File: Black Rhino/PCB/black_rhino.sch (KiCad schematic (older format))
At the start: 174 parts, among them SW1 SW_Push, U1 ATmega32U4-AU, Y1 16MHz

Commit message: Improve Black Rhino-PCB
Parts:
- added H23: MountingHole, MountingHole:MountingHole_2mm, symbol Mechanical:MountingHole
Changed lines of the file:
@@
 Wire Wire Line
 	19900 2900 20650 2900
+$Comp
+L Mechanical:MountingHole H23
+U 1 1 5F2CFA80
+P 19300 13400
+F 0 "H23" H 19400 13446 50  0000 L CNN
+F 1 "MountingHole" H 19400 13355 50  0000 L CNN
+F 2 "MountingHole:MountingHole_2mm" H 19300 13400 50  0001 C CNN
+F 3 "~" H 19300 13400 50  0001 C CNN
+	1    19300 13400
+	1    0    0    -1
+$EndComp
 $EndSCHEMATC

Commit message: Improve Black Rhino-PCB
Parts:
- removed H13, H14, H15, H16, H17, H18, H19, H20, H21, H22, H23: MountingHole, MountingHole:MountingHole_2mm, symbol Mechanical:MountingHole
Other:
- moved on the sheet: H10, H11, H12, H7, H8, H9
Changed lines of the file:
@@
 L Mechanical:MountingHole H7
 U 1 1 5F2A8030
-P 19300 12150
-F 0 "H7" H 19400 12196 50  0000 L CNN
-F 1 "MountingHole" H 19400 12105 50  0000 L CNN
-F 2 "MountingHole:MountingHole_2mm" H 19300 12150 50  0001 C CNN
-F 3 "~" H 19300 12150 50  0001 C CNN
-	1    19300 12150
+P 20100 10650
+F 0 "H7" H 20200 10696 50  0000 L CNN
+F 1 "MountingHole" H 20200 10605 50  0000 L CNN
+F 2 "MountingHole:MountingHole_2mm" H 20100 10650 50  0001 C CNN
+F 3 "~" H 20100 10650 50  0001 C CNN
+	1    20100 10650
 	1    0    0    -1
 $EndComp
@@
 L Mechanical:MountingHole H8
 U 1 1 5F2B82E0
-P 19300 12400
-F 0 "H8" H 19400 12446 50  0000 L CNN
-F 1 "MountingHole" H 19400 12355 50  0000 L CNN
-F 2 "MountingHole:MountingHole_2mm" H 19300 12400 50  0001 C CNN
-F 3 "~" H 19300 12400 50  0001 C CNN
-	1    19300 12400
+P 20100 10900
+F 0 "H8" H 20200 10946 50  0000 L CNN
+F 1 "MountingHole" H 20200 10855 50  0000 L CNN
+F 2 "MountingHole:MountingHole_2mm" H 20100 10900 50  0001 C CNN
+F 3 "~" H 20100 10900 50  0001 C CNN
+	1    20100 10900
 	1    0    0    -1
 $EndComp
@@
 L Mechanical:MountingHole H9
 U 1 1 5F316618
-P 20300 10650
-F 0 "H9" H 20400 10696 50  0000 L CNN
-F 1 "MountingHole" H 20400 10605 50  0000 L CNN
-F 2 "MountingHole:MountingHole_2mm" H 20300 10650 50  0001 C CNN
-F 3 "~" H 20300 10650 50  0001 C CNN
-	1    20300 10650
+P 20100 11150
+F 0 "H9" H 20200 11196 50  0000 L CNN
+F 1 "MountingHole" H 20200 11105 50  0000 L CNN
+F 2 "MountingHole:MountingHole_2mm" H 20100 11150 50  0001 C CNN
+F 3 "~" H 20100 11150 50  0001 C CNN
+	1    20100 11150
 	1    0    0    -1
 $EndComp
@@
 L Mechanical:MountingHole H10
 U 1 1 5F31661E
-P 20300 10900
-F 0 "H10" H 20400 10946 50  0000 L CNN
-F 1 "MountingHole" H 20400 10855 50  0000 L CNN
-F 2 "MountingHole:MountingHole_2mm" H 20300 10900 50  0001 C CNN
-F 3 "~" H 20300 10900 50  0001 C CNN
-	1    20300 10900
+P 20100 11400
+F 0 "H10" H 20200 11446 50  0000 L CNN
+F 1 "MountingHole" H 20200 11355 50  0000 L CNN
+F 2 "MountingHole:MountingHole_2mm" H 20100 11400 50  0001 C CNN
+F 3 "~" H 20100 11400 50  0001 C CNN
+	1    20100 11400
 	1    0    0    -1
 $EndComp
@@
 L Mechanical:MountingHole H11
 U 1 1 5F316624
-P 20300 11150
-F 0 "H11" H 20400 11196 50  0000 L CNN
-F 1 "MountingHole" H 20400 11105 50  0000 L CNN
-F 2 "MountingHole:MountingHole_2mm" H 20300 11150 50  0001 C CNN
-F 3 "~" H 20300 11150 50  0001 C CNN
-	1    20300 11150
+P 20100 11650
+F 0 "H11" H 20200 11696 50  0000 L CNN
+F 1 "MountingHole" H 20200 11605 50  0000 L CNN
+F 2 "MountingHole:MountingHole_2mm" H 20100 11650 50  0001 C CNN
+F 3 "~" H 20100 11650 50  0001 C CNN
+	1    20100 11650
 	1    0    0    -1
 $EndComp
@@
 L Mechanical:MountingHole H12
 U 1 1 5F31662A
-P 20300 11400
-F 0 "H12" H 20400 11446 50  0000 L CNN
-F 1 "MountingHole" H 20400 11355 50  0000 L CNN
-F 2 "MountingHole:MountingHole_2mm" H 20300 11400 50  0001 C CNN
-F 3 "~" H 20300 11400 50  0001 C CNN
-	1    20300 11400
-	1    0    0    -1
-$EndComp
-$Comp
-L Mechanical:MountingHole H13
-U 1 1 5F316630
-P 20300 11650
-F 0 "H13" H 20400 11696 50  0000 L CNN
-F 1 "MountingHole" H 20400 11605 50  0000 L CNN
-F 2 "MountingHole:MountingHole_2mm" H 20300 11650 50  0001 C CNN
-F 3 "~" H 20300 11650 50  0001 C CNN
-	1    20300 11650
-	1    0    0    -1
-$EndComp
-$Comp
-L Mechanical:MountingHole H14
-U 1 1 5F316636
-P 20300 11900
-F 0 "H14" H 20400 11946 50  0000 L CNN
-F 1 "MountingHole" H 20400 11855 50  0000 L CNN
-F 2 "MountingHole:MountingHole_2mm" H 20300 11900 50  0001 C CNN
-F 3 "~" H 20300 11900 50  0001 C CNN
-	1    20300 11900
-	1    0    0    -1
-$EndComp
-$Comp
-L Mechanical:MountingHole H15
-U 1 1 5F31663C
-P 20300 12150
-F 0 "H15" H 20400 12196 50  0000 L CNN
-F 1 "MountingHole" H 20400 12105 50  0000 L CNN
-F 2 "MountingHole:MountingHole_2mm" H 20300 12150 50  0001 C CNN
-F 3 "~" H 20300 12150 50  0001 C CNN
-	1    20300 12150
-	1    0    0    -1
-$EndComp
-$Comp
-L Mechanical:MountingHole H16
-U 1 1 5F316642
-P 20300 12400
-F 0 "H16" H 20400 12446 50  0000 L CNN
-F 1 "MountingHole" H 20400 12355 50  0000 L CNN
-F 2 "MountingHole:MountingHole_2mm" H 20300 12400 50  0001 C CNN
-F 3 "~" H 20300 12400 50  0001 C CNN
-	1    20300 12400
-	1    0    0    -1
-$EndComp
-$Comp
-L Mechanical:MountingHole H17
-U 1 1 5F34FFBE
-P 19300 12650
-F 0 "H17" H 19400 12696 50  0000 L CNN
-F 1 "MountingHole" H 19400 12605 50  0000 L CNN
-F 2 "MountingHole:MountingHole_2mm" H 19300 12650 50  0001 C CNN
-F 3 "~" H 19300 12650 50  0001 C CNN
-	1    19300 12650
-	1    0    0    -1
-$EndComp
-$Comp
-L Mechanical:MountingHole H18
-U 1 1 5F34FFC4
-P 20300 12650
-F 0 "H18" H 20400 12696 50  0000 L CNN
-F 1 "MountingHole" H 20400 12605 50  0000 L CNN
-F 2 "MountingHole:MountingHole_2mm" H 20300 12650 50  0001 C CNN
-F 3 "~" H 20300 12650 50  0001 C CNN
-	1    20300 12650
-	1    0    0    -1
-$EndComp
-$Comp
-L Mechanical:MountingHole H19
-U 1 1 5F37F0C0
-P 19300 12900
-F 0 "H19" H 19400 12946 50  0000 L CNN
-F 1 "MountingHole" H 19400 12855 50  0000 L CNN
-F 2 "MountingHole:MountingHole_2mm" H 19300 12900 50  0001 C CNN
-F 3 "~" H 19300 12900 50  0001 C CNN
-	1    19300 12900
-	1    0    0    -1
-$EndComp
-$Comp
-L Mechanical:MountingHole H20
-U 1 1 5F37F0C6
-P 20300 12900
-F 0 "H20" H 20400 12946 50  0000 L CNN
-F 1 "MountingHole" H 20400 12855 50  0000 L CNN
-F 2 "MountingHole:MountingHole_2mm" H 20300 12900 50  0001 C CNN
-F 3 "~" H 20300 12900 50  0001 C CNN
-	1    20300 12900
-	1    0    0    -1
-$EndComp
-$Comp
-L Mechanical:MountingHole H21
-U 1 1 5F3B30CA
-P 19300 13150
-F 0 "H21" H 19400 13196 50  0000 L CNN
-F 1 "MountingHole" H 19400 13105 50  0000 L CNN
-F 2 "MountingHole:MountingHole_2mm" H 19300 13150 50  0001 C CNN
-F 3 "~" H 19300 13150 50  0001 C CNN
-	1    19300 13150
-	1    0    0    -1
-$EndComp
-$Comp
-L Mechanical:MountingHole H22
-U 1 1 5F251A42
-P 20300 13150
-F 0 "H22" H 20400 13196 50  0000 L CNN
-F 1 "MountingHole" H 20400 13105 50  0000 L CNN
-F 2 "MountingHole:MountingHole_2mm" H 20300 13150 50  0001 C CNN
-F 3 "~" H 20300 13150 50  0001 C CNN
-	1    20300 13150
+P 20100 11900
+F 0 "H12" H 20200 11946 50  0000 L CNN
+F 1 "MountingHole" H 20200 11855 50  0000 L CNN
+F 2 "MountingHole:MountingHole_2mm" H 20100 11900 50  0001 C CNN
+F 3 "~" H 20100 11900 50  0001 C CNN
+	1    20100 11900
 	1    0    0    -1
 $EndComp
@@
 Wire Wire Line
 	19900 2900 20650 2900
-$Comp
-L Mechanical:MountingHole H23
-U 1 1 5F2CFA80
-P 19300 13400
-F 0 "H23" H 19400 13446 50  0000 L CNN
-F 1 "MountingHole" H 19400 13355 50  0000 L CNN
-F 2 "MountingHole:MountingHole_2mm" H 19300 13400 50  0001 C CNN
-F 3 "~" H 19300 13400 50  0001 C CNN
-	1    19300 13400
-	1    0    0    -1
-$EndComp
 $EndSCHEMATC

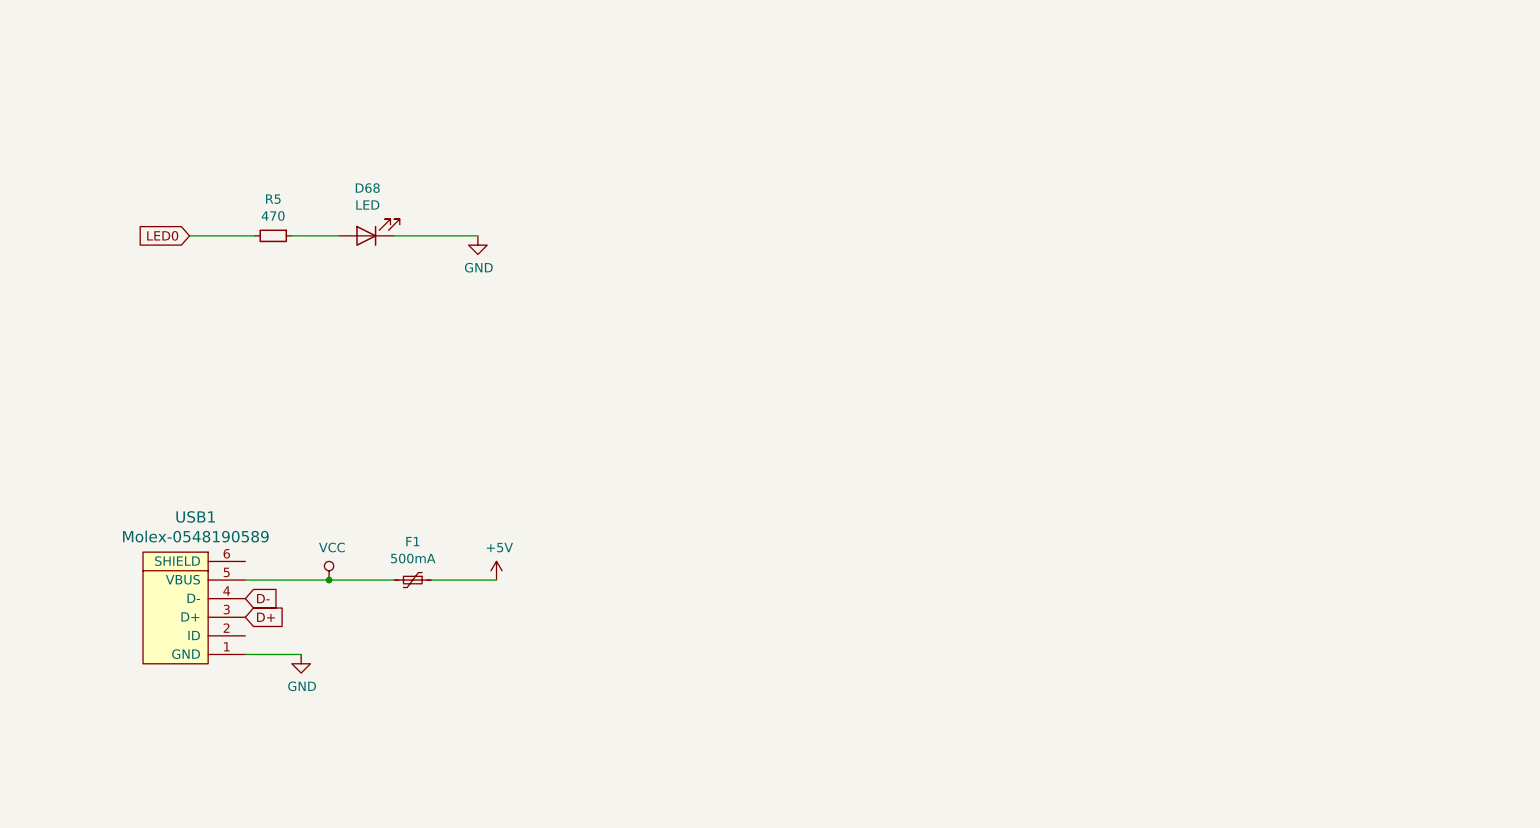
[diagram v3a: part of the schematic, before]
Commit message: Add USB-C to Black Rhino
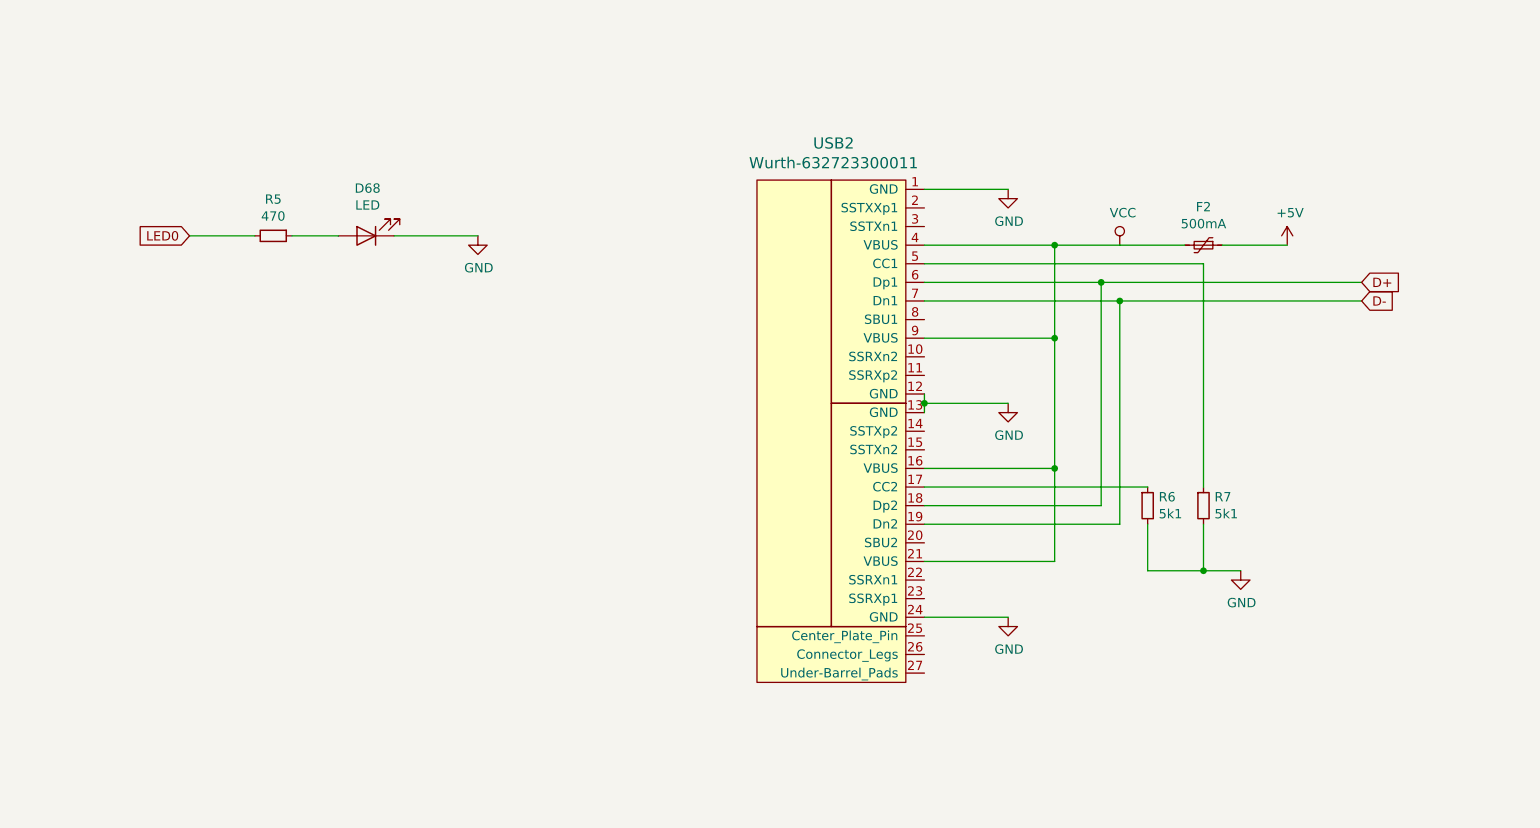
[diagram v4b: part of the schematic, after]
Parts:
- removed F1: 500mA, Fuse:Fuse_1206_3216Metric, symbol Device:Polyfuse_Small
- removed USB1: Molex-0548190589, random-keyboard-parts:Molex-0548190589, symbol random-keyboard-parts:Molex-0548190589
- added F2: 500mA, Fuse:Fuse_1206_3216Metric, symbol Device:Polyfuse_Small
- added R6, R7: 5k1, Resistor_SMD:R_0805_2012Metric, symbol Device:R_Small
- added USB2: Wurth-632723300011, Type-C:Wurth-632723300011, symbol Type-C:Wurth-632723300011
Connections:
- net +5V: now also F2.1
- net D+: now also USB2.18 (Dp2), USB2.6 (Dp1)
- net D-: now also USB2.19 (Dn2), USB2.7 (Dn1)
- net GND: now also R6.2, R7.2, USB2.1 (GND), USB2.12 (GND), USB2.13 (GND), USB2.24 (GND)
- net VCC: now also F2.2, USB2.16 (VBUS), USB2.21 (VBUS), USB2.4 (VBUS), USB2.9 (VBUS)
- new net: R6.1, USB2.17 (CC2)
- new net: R7.1, USB2.5 (CC1)
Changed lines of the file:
@@
 COL0
-Wire Wire Line
-	3250 10050 3550 10050
-$Comp
-L power:GND #PWR0113
-U 1 1 5F26C44D
-P 3550 10050
-F 0 "#PWR0113" H 3550 9800 50  0001 C CNN
-F 1 "GND" H 3555 9877 50  0000 C CNN
-F 2 "" H 3550 10050 50  0001 C CNN
-F 3 "" H 3550 10050 50  0001 C CNN
-	1    3550 10050
-	1    0    0    -1
-$EndComp
-Text GLabel 3250 9850 2    50   Input ~ 0
-D+
-Text GLabel 3250 9750 2    50   Input ~ 0
-D-
-Wire Wire Line
-	4600 9650 4250 9650
-$Comp
-L power:+5V #PWR0112
-U 1 1 5F26AF92
-P 4600 9650
-F 0 "#PWR0112" H 4600 9500 50  0001 C CNN
-F 1 "+5V" H 4615 9823 50  0000 C CNN
-F 2 "" H 4600 9650 50  0001 C CNN
-F 3 "" H 4600 9650 50  0001 C CNN
-	1    4600 9650
-	1    0    0    -1
-$EndComp
-Connection ~ 3700 9650
-Wire Wire Line
-	4050 9650 3700 9650
-$Comp
-L Device:Polyfuse_Small F1
-U 1 1 5F269C41
-P 4150 9650
-F 0 "F1" V 3945 9650 50  0000 C CNN
-F 1 "500mA" V 4036 9650 50  0000 C CNN
-F 2 "Fuse:Fuse_1206_3216Metric" H 4200 9450 50  0001 L CNN
-F 3 "~" H 4150 9650 50  0001 C CNN
-	1    4150 9650
-	0    1    1    0
-$EndComp
-Wire Wire Line
-	3250 9650 3700 9650
-$Comp
-L power:VCC #PWR0111
-U 1 1 5F268111
-P 3700 9650
-F 0 "#PWR0111" H 3700 9500 50  0001 C CNN
-F 1 "VCC" H 3717 9823 50  0000 C CNN
-F 2 "" H 3700 9650 50  0001 C CNN
-F 3 "" H 3700 9650 50  0001 C CNN
-	1    3700 9650
-	1    0    0    -1
-$EndComp
-$Comp
-L random-keyboard-parts:Molex-0548190589 USB1
-U 1 1 5F267617
-P 2950 9850
-F 0 "USB1" V 3487 9817 60  0000 C CNN
-F 1 "Molex-0548190589" V 3381 9817 60  0000 C CNN
-F 2 "random-keyboard-parts:Molex-0548190589" H 2950 9850 60  0001 C CNN
-F 3 "" H 2950 9850 60  0001 C CNN
-	1    2950 9850
-	0    -1   -1   0
-$EndComp
 Wire Wire Line
 	4050 1500 4050 1650
@@
 	-1   0    0    1
 $EndComp
+$Comp
+L power:GND #PWR0115
+U 1 1 5F3AC971
+P 7350 7550
+F 0 "#PWR0115" H 7350 7300 50  0001 C CNN
+F 1 "GND" H 7355 7377 50  0000 C CNN
+F 2 "" H 7350 7550 50  0001 C CNN
+F 3 "" H 7350 7550 50  0001 C CNN
+	1    7350 7550
+	1    0    0    -1
+$EndComp
+Wire Wire Line
+	6900 8750 6900 8700
+$Comp
+L power:GND #PWR0116
+U 1 1 5F3D340E
+P 7350 8700
+F 0 "#PWR0116" H 7350 8450 50  0001 C CNN
+F 1 "GND" H 7355 8527 50  0000 C CNN
+F 2 "" H 7350 8700 50  0001 C CNN
+F 3 "" H 7350 8700 50  0001 C CNN
+	1    7350 8700
+	1    0    0    -1
+$EndComp
+$Comp
+L power:GND #PWR0117
+U 1 1 5F3E6939
+P 7350 9850
+F 0 "#PWR0117" H 7350 9600 50  0001 C CNN
+F 1 "GND" H 7355 9677 50  0000 C CNN
+F 2 "" H 7350 9850 50  0001 C CNN
+F 3 "" H 7350 9850 50  0001 C CNN
+	1    7350 9850
+	1    0    0    -1
+$EndComp
+Wire Wire Line
+	6900 9850 7350 9850
+Wire Wire Line
+	6900 7550 7350 7550
+Wire Wire Line
+	6900 8700 7350 8700
+Connection ~ 6900 8700
+Wire Wire Line
+	6900 8700 6900 8650
+$Comp
+L power:VCC #PWR0118
+U 1 1 5F49CF34
+P 7950 7850
+F 0 "#PWR0118" H 7950 7700 50  0001 C CNN
+F 1 "VCC" H 7967 8023 50  0000 C CNN
+F 2 "" H 7950 7850 50  0001 C CNN
+F 3 "" H 7950 7850 50  0001 C CNN
+	1    7950 7850
+	1    0    0    -1
+$EndComp
+Wire Wire Line
+	6900 9050 7600 9050
+Wire Wire Line
+	7600 9050 7600 8350
+Wire Wire Line
+	7600 7850 7950 7850
+$Comp
+L Type-C:Wurth-632723300011 USB2
+U 1 1 5F3AA4EB
+P 6800 8700
+F 0 "USB2" H 6412 10097 60  0000 C CNN
+F 1 "Wurth-632723300011" H 6412 9991 60  0000 C CNN
+F 2 "Type-C:Wurth-632723300011" H 6800 8700 60  0001 C CNN
+F 3 "" H 6800 8700 60  0001 C CNN
+	1    6800 8700
+	1    0    0    -1
+$EndComp
+Wire Wire Line
+	7600 7850 6900 7850
+Connection ~ 7600 7850
+$Comp
+L Device:R_Small R6
+U 1 1 5F67607D
+P 8100 9250
+F 0 "R6" H 8159 9296 50  0000 L CNN
+F 1 "5k1" H 8159 9205 50  0000 L CNN
+F 2 "Resistor_SMD:R_0805_2012Metric" H 8100 9250 50  0001 C CNN
+F 3 "~" H 8100 9250 50  0001 C CNN
+	1    8100 9250
+	1    0    0    -1
+$EndComp
+Wire Wire Line
+	6900 9150 8100 9150
+$Comp
+L Device:R_Small R7
+U 1 1 5F6A1B1B
+P 8400 9250
+F 0 "R7" H 8459 9296 50  0000 L CNN
+F 1 "5k1" H 8459 9205 50  0000 L CNN
+F 2 "Resistor_SMD:R_0805_2012Metric" H 8400 9250 50  0001 C CNN
+F 3 "~" H 8400 9250 50  0001 C CNN
+	1    8400 9250
+	1    0    0    -1
+$EndComp
+Wire Wire Line
+	8100 9350 8100 9600
+Wire Wire Line
+	8100 9600 8400 9600
+Wire Wire Line
+	8400 9600 8400 9350
+Wire Wire Line
+	8400 9600 8600 9600
+Connection ~ 8400 9600
+$Comp
+L power:GND #PWR0119
+U 1 1 5F6EF5B8
+P 8600 9600
+F 0 "#PWR0119" H 8600 9350 50  0001 C CNN
+F 1 "GND" H 8605 9427 50  0000 C CNN
+F 2 "" H 8600 9600 50  0001 C CNN
+F 3 "" H 8600 9600 50  0001 C CNN
+	1    8600 9600
+	1    0    0    -1
+$EndComp
+Wire Wire Line
+	8400 9150 8400 7950
+Wire Wire Line
+	8400 7950 6900 7950
+Wire Wire Line
+	6900 8350 7600 8350
+Connection ~ 7600 8350
+Wire Wire Line
+	7600 8350 7600 7850
+Wire Wire Line
+	6900 9550 7600 9550
+Wire Wire Line
+	7600 9550 7600 9050
+Connection ~ 7600 9050
+Wire Wire Line
+	8850 7850 8500 7850
+$Comp
+L power:+5V #PWR0120
+U 1 1 5F84C51A
+P 8850 7850
+F 0 "#PWR0120" H 8850 7700 50  0001 C CNN
+F 1 "+5V" H 8865 8023 50  0000 C CNN
+F 2 "" H 8850 7850 50  0001 C CNN
+F 3 "" H 8850 7850 50  0001 C CNN
+	1    8850 7850
+	1    0    0    -1
+$EndComp
+Wire Wire Line
+	8300 7850 7950 7850
+$Comp
+L Device:Polyfuse_Small F2
+U 1 1 5F84C521
+P 8400 7850
+F 0 "F2" V 8195 7850 50  0000 C CNN
+F 1 "500mA" V 8286 7850 50  0000 C CNN
+F 2 "Fuse:Fuse_1206_3216Metric" H 8450 7650 50  0001 L CNN
+F 3 "~" H 8400 7850 50  0001 C CNN
+	1    8400 7850
+	0    1    1    0
+$EndComp
+Wire Wire Line
+	6900 8050 7850 8050
+Wire Wire Line
+	6900 9250 7850 9250
+Wire Wire Line
+	7850 9250 7850 8050
+Wire Wire Line
+	6900 8150 7950 8150
+Wire Wire Line
+	6900 9350 7950 9350
+Wire Wire Line
+	7950 9350 7950 8150
+Connection ~ 7950 8150
+Wire Wire Line
+	7950 8150 9250 8150
+Text GLabel 9250 8050 2    50   Input ~ 0
+D+
+Text GLabel 9250 8150 2    50   Input ~ 0
+D-
+Wire Wire Line
+	7850 8050 9250 8050
+Connection ~ 7850 8050
 $EndSCHEMATC

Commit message: Update Black Rhino-PCB
USB-C from commit
4d49d241aeb4ff990ef37ecb95a9e68bcacd4131
is implemented with this commit.
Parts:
- removed F2: 500mA, Fuse:Fuse_1206_3216Metric, symbol Device:Polyfuse_Small
- removed USB2: Wurth-632723300011, Type-C:Wurth-632723300011, symbol Type-C:Wurth-632723300011
- added F1: 500mA, Fuse:Fuse_1206_3216Metric, symbol Device:Polyfuse_Small
- added USB1: GCT-USB4085-GF-A, Type-C:USB_C_GCT_USB4085, symbol Type-C:GCT-USB4085-GF-A
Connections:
- net +5V: now also F1.1
- net D+: now also USB1.A6 (Dp1), USB1.B6 (Dp2)
- net D-: now also USB1.A7 (Dn1), USB1.B7 (Dn2)
- net GND: now also USB1.A1 (GND), USB1.A12 (GND), USB1.B1 (GND), USB1.B12 (GND), USB1.S1 (GND)
- net VCC: now also F1.2, USB1.A4 (VBUS), USB1.A9 (VBUS), USB1.B4 (VBUS), USB1.B9 (VBUS)
- net at R6.1: now also USB1.A5 (CC1)
- net at R7.1: now also USB1.B5 (CC2)
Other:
- moved on the sheet: C4, C5, C6, C7, D68, H1, H10, H11, H12, H2, H3, H4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
